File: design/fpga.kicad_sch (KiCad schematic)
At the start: 83 parts, among them J7 DEBUG_FPGA_GPIO, J8 DIGILENT_JTAG_HS2_01X06, SW1 RST, SW2 PROG, U13 XC7S15-FTGB196, U14 IS25LP064A-JKx

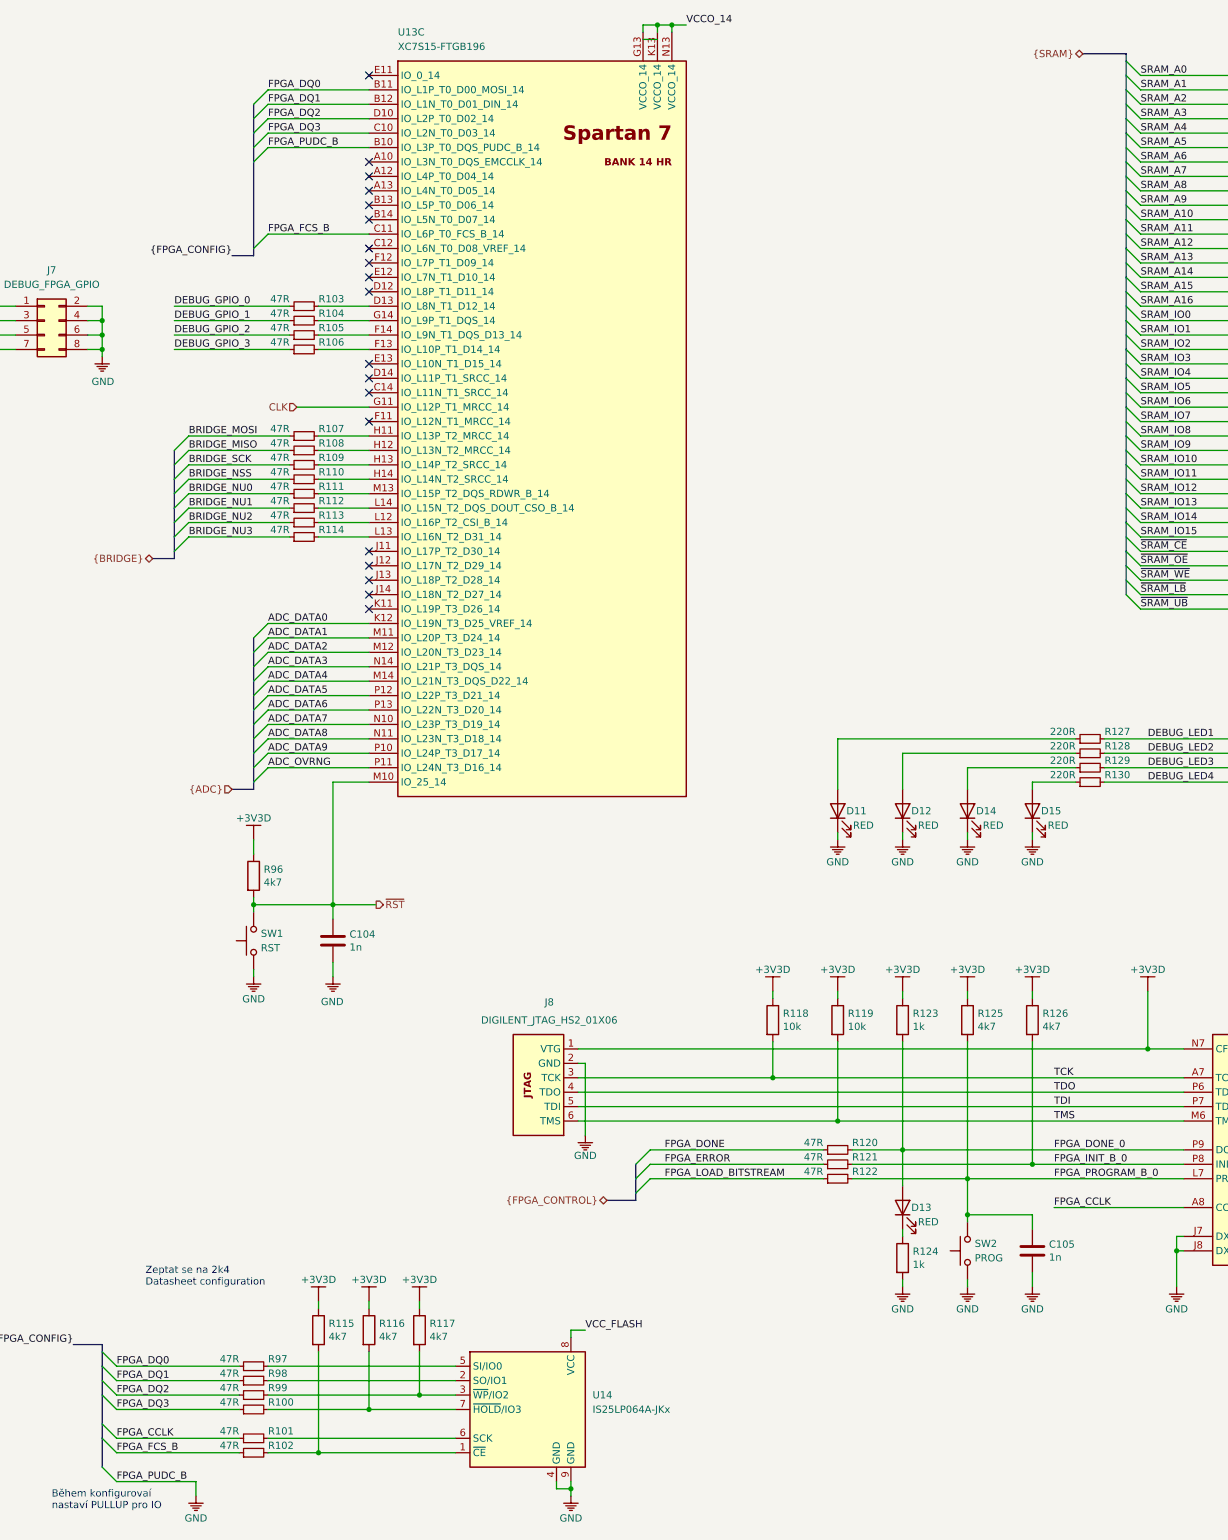
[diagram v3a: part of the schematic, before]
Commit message: Added buses that were removed when converting from the old format
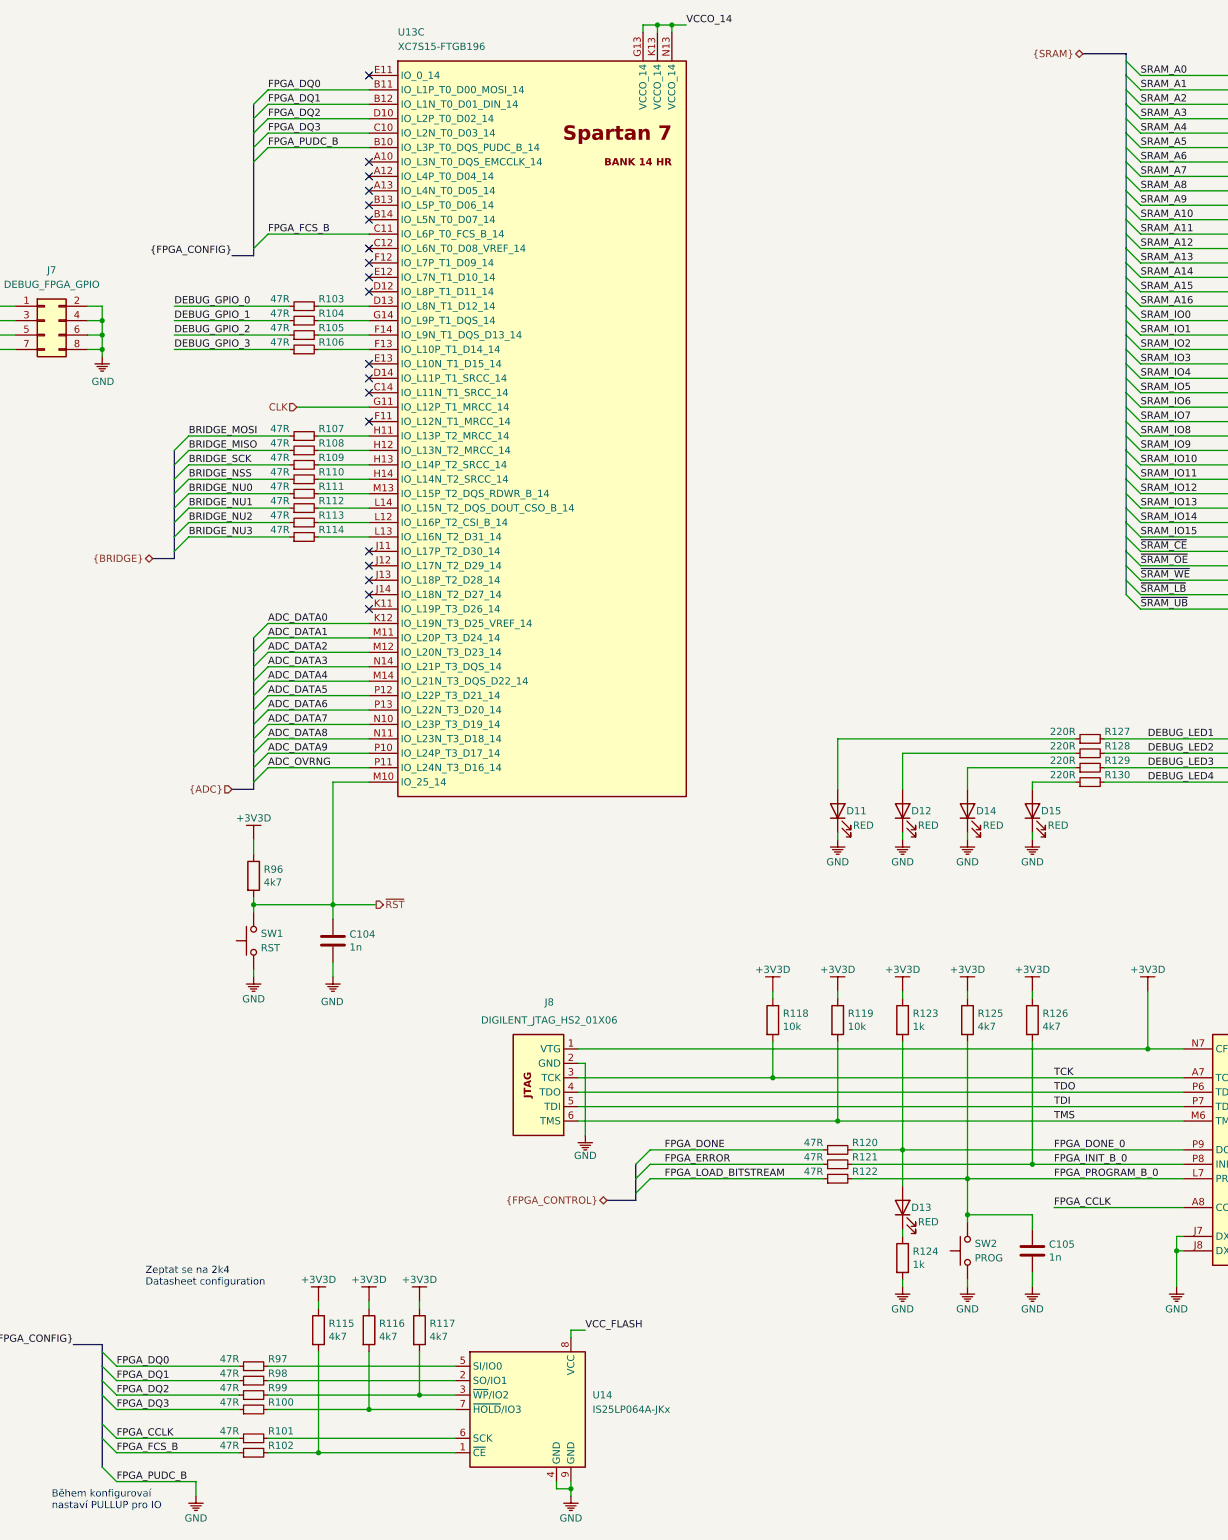
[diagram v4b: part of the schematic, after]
